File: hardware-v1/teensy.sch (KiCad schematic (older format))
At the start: 31 parts, among them J1 USB-MICRO-B-SHIELDED, P7 USB_POWER, P8 CORTEX_DEBUG, SW2 PROGRAM, U4 LP38691, U5 MK20DX256VLH7, U6 MKL02Z32VFG4, X1 CRYSTAL_SMD, Y1 32kHz

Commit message: Finalizing revB
 - Added part numbers on all parts (in kicad PartNumber field)
 - Some finicking in a bunch of corners
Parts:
- C10, C4, C5, C6: PartNumber (none) -> CC0603MRX5R5BB225
- C11, C12, C13, C14, C7, C8, C9: PartNumber (none) -> CC0603KPX7R7BB104
- D3: PartNumber (none) -> LTST-C190KFKT
- D4: PartNumber (none) -> LM4040QCEM3-3.0/NOPB
- J1: PartNumber (none) -> 10103592-0001LF
- L2, L3, L4: PartNumber (none) -> 742792651
- P7: PartNumber (none) -> PREC002SAAN-RC
- P8: PartNumber (none) -> 3220-10-0100-00
- R10: PartNumber (none) -> RC0603JR-072K4L
- R11: PartNumber (none) -> RC0603JR-07470RL
- R12: PartNumber (none) -> 311-0.0HRCT-ND
- R8, R9: PartNumber (none) -> RC0603JR-0733RL
- SW2: PartNumber (none) -> FSMSM
- U4: PartNumber (none) -> LP38691DTX-3.3/NOPB
- U5: PartNumber (none) -> MK20DX256VLH7
- X1: PartNumber (none) -> NX3225SA-16.000MHZ-STD-CSR-1
- Y1: PartNumber (none) -> CFV-20632000AZFB
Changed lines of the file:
@@
 F 2 "Housings_QFP:TQFP-64_10x10mm_Pitch0.5mm" H 8350 3550 60  0001 C CNN
 F 3 "" H 8350 3550 60  0000 C CNN
+F 4 "MK20DX256VLH7" H 7650 3300 60  0001 C CNN "PartNumber"
 	1    7650 3300
 	1    0    0    -1
@@
 F 2 "bb:SWITCH_SMD_3x6" H 3750 4900 60  0001 C CNN
 F 3 "" H 3750 4900 60  0000 C CNN
+F 4 "FSMSM" H 3750 4900 60  0001 C CNN "PartNumber"
 	1    3750 4900
 	1    0    0    -1
@@
 F 2 "bb:HEADER_2x5_0.05" H 2450 5000 60  0001 C CNN
 F 3 "" H 2450 5000 60  0000 C CNN
+F 4 "3220-10-0100-00" H 2450 6200 60  0001 C CNN "PartNumber"
 	1    2450 6200
 	1    0    0    -1
@@
 F 2 "Resistors_SMD:R_0603" V 1930 1350 30  0001 C CNN
 F 3 "" H 2000 1350 30  0000 C CNN
+F 4 "RC0603JR-0733RL" H 2000 1350 60  0001 C CNN "PartNumber"
 	1    2000 1350
 	0    -1   -1   0
@@
 F 2 "Resistors_SMD:R_0603" V 1930 1500 30  0001 C CNN
 F 3 "" H 2000 1500 30  0000 C CNN
+F 4 "RC0603JR-0733RL" H 2000 1500 60  0001 C CNN "PartNumber"
 	1    2000 1500
 	0    -1   -1   0
@@
 F 2 "Resistors_SMD:R_0603" H 1300 2050 60  0001 C CNN
 F 3 "" H 1300 2050 60  0000 C CNN
+F 4 "742792651" H 1300 2050 60  0001 C CNN "PartNumber"
 	1    1300 2050
 	0    1    1    0
@@
 F 2 "Capacitors_SMD:C_0603" H 6200 1600 60  0001 C CNN
 F 3 "" H 6200 1600 60  0000 C CNN
+F 4 "CC0603MRX5R5BB225" H 6200 1600 60  0001 C CNN "PartNumber"
 	1    6200 1600
 	1    0    0    -1
@@
 F 2 "Capacitors_SMD:C_0603" H 6000 1600 60  0001 C CNN
 F 3 "" H 6000 1600 60  0000 C CNN
+F 4 "CC0603KPX7R7BB104" H 6000 1600 60  0001 C CNN "PartNumber"
 	1    6000 1600
 	1    0    0    -1
@@
 F 2 "Capacitors_SMD:C_0603" H 5800 1600 60  0001 C CNN
 F 3 "" H 5800 1600 60  0000 C CNN
+F 4 "CC0603KPX7R7BB104" H 5800 1600 60  0001 C CNN "PartNumber"
 	1    5800 1600
 	1    0    0    -1
@@
 F 2 "Capacitors_SMD:C_0603" H 5600 1600 60  0001 C CNN
 F 3 "" H 5600 1600 60  0000 C CNN
+F 4 "CC0603KPX7R7BB104" H 5600 1600 60  0001 C CNN "PartNumber"
 	1    5600 1600
 	1    0    0    -1
@@
 F 2 "Resistors_SMD:R_0603" H 5200 1800 60  0001 C CNN
 F 3 "" H 5200 1800 60  0000 C CNN
+F 4 "742792651" H 5200 1800 60  0001 C CNN "PartNumber"
 	1    5200 1800
 	-1   0    0    1
@@
 F 2 "Resistors_SMD:R_0603" H 5300 3000 60  0001 C CNN
 F 3 "" H 5300 3000 60  0000 C CNN
+F 4 "742792651" H 5300 3000 60  0001 C CNN "PartNumber"
 	1    5300 3000
 	-1   0    0    1
@@
 F 2 "Resistors_SMD:R_0603" V 5630 2400 30  0001 C CNN
 F 3 "" H 5700 2400 30  0000 C CNN
+F 4 "RC0603JR-072K4L" H 5700 2400 60  0001 C CNN "PartNumber"
 	1    5700 2400
 	0    1    1    0
@@
 F 2 "Capacitors_SMD:C_0603" H 6450 2550 60  0001 C CNN
 F 3 "" H 6450 2550 60  0000 C CNN
+F 4 "CC0603KPX7R7BB104" H 6450 2550 60  0001 C CNN "PartNumber"
 	1    6450 2550
 	1    0    0    -1
@@
 F 2 "Capacitors_SMD:C_0603" H 5400 2550 60  0001 C CNN
 F 3 "" H 5400 2550 60  0000 C CNN
+F 4 "CC0603KPX7R7BB104" H 5400 2550 60  0001 C CNN "PartNumber"
 	1    5400 2550
 	1    0    0    -1
@@
 F 2 "bb:Crystal_Watch_6mm" H 6800 3400 60  0001 C CNN
 F 3 "" H 6800 3400 60  0000 C CNN
+F 4 "CFV-20632000AZFB" H 6800 3400 60  0001 C CNN "PartNumber"
 	1    6800 3400
 	0    1    1    0
@@
 F 2 "TO_SOT_Packages_SMD:TO-252-2Lead" H 3550 1400 60  0001 C CNN
 F 3 "" H 3550 1400 60  0000 C CNN
+F 4 "LP38691DTX-3.3/NOPB" H 3550 1400 60  0001 C CNN "PartNumber"
 	1    3550 1400
 	1    0    0    -1
@@
 F 2 "Capacitors_SMD:C_0603" H 4100 1550 60  0001 C CNN
 F 3 "" H 4100 1550 60  0000 C CNN
+F 4 "CC0603MRX5R5BB225" H 4100 1550 60  0001 C CNN "PartNumber"
 	1    4100 1550
 	1    0    0    -1
@@
 F 2 "Capacitors_SMD:C_0603" H 3000 1550 60  0001 C CNN
 F 3 "" H 3000 1550 60  0000 C CNN
+F 4 "CC0603MRX5R5BB225" H 3000 1550 60  0001 C CNN "PartNumber"
 	1    3000 1550
 	1    0    0    -1
@@
 F 2 "Capacitors_SMD:C_0603" H 1500 1050 60  0001 C CNN
 F 3 "" H 1500 1050 60  0000 C CNN
+F 4 "CC0603MRX5R5BB225" H 1500 1050 60  0001 C CNN "PartNumber"
 	1    1500 1050
 	1    0    0    -1
@@
 F 2 "LEDs:LED_0603" H 9450 2500 60  0001 C CNN
 F 3 "" H 9450 2500 60  0000 C CNN
+F 4 "LTST-C190KFKT" H 9450 2500 60  0001 C CNN "PartNumber"
 	1    9450 2500
 	-1   0    0    1
@@
 F 2 "Resistors_SMD:R_0603" V 9830 2500 30  0001 C CNN
 F 3 "" H 9900 2500 30  0000 C CNN
+F 4 "RC0603JR-07470RL" H 9900 2500 60  0001 C CNN "PartNumber"
 	1    9900 2500
 	0    -1   -1   0
@@
 F 2 "Pin_Headers:Pin_Header_Straight_1x02" H 1900 700 60  0001 C CNN
 F 3 "" H 1900 700 60  0000 C CNN
+F 4 "PREC002SAAN-RC" H 1900 700 60  0001 C CNN "PartNumber"
 	1    1900 700
 	0    -1   -1   0
@@
 F 2 "Capacitors_SMD:C_0603" H 5750 3500 60  0001 C CNN
 F 3 "" H 5750 3500 60  0000 C CNN
+F 4 "CC0603KPX7R7BB104" H 5750 3500 60  0001 C CNN "PartNumber"
 	1    5750 3500
 	1    0    0    -1
@@
 F 2 "gsg-modules:USB-MICROB-FCI-10103592-LONGPADS" H 1000 1450 60  0001 C CNN
 F 3 "" H 1000 1450 60  0000 C CNN
+F 4 "10103592-0001LF" H 1000 1450 60  0001 C CNN "PartNumber"
 	1    1000 1450
 	-1   0    0    -1
@@
 F 2 "bb:CRYSTAL-NX3225SA" H 6600 3100 60  0001 C CNN
 F 3 "" H 6600 3100 60  0000 C CNN
+F 4 "NX3225SA-16.000MHZ-STD-CSR-1" H 6600 3100 60  0001 C CNN "PartNumber"
 	1    6600 3100
 	1    0    0    -1
@@
 F 2 "Capacitors_SMD:C_0603" H 1350 3750 60  0001 C CNN
 F 3 "" H 1350 3750 60  0000 C CNN
+F 4 "CC0603KPX7R7BB104" H 1350 3750 60  0001 C CNN "PartNumber"
 	1    1350 3750
 	1    0    0    -1
@@
 F 2 "Resistors_SMD:R_0603" V 3180 3600 50  0001 C CNN
 F 3 "" H 3250 3600 50  0000 C CNN
+F 4 "311-0.0HRCT-ND " H 3250 3600 60  0001 C CNN "PartNumber"
 	1    3250 3600
 	0    1    1    0
@@
 F 2 "TO_SOT_Packages_SMD:SOT-23" H 6050 2550 50  0001 C CNN
 F 3 "" H 6050 2550 50  0000 C CNN
+F 4 "LM4040QCEM3-3.0/NOPB" H 6050 2550 60  0001 C CNN "PartNumber"
 	1    6050 2550
 	0    1    1    0

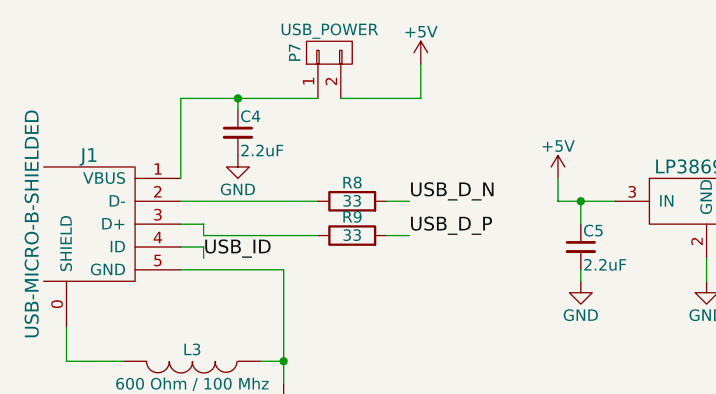
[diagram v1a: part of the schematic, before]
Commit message: adding oring diodes to schematic
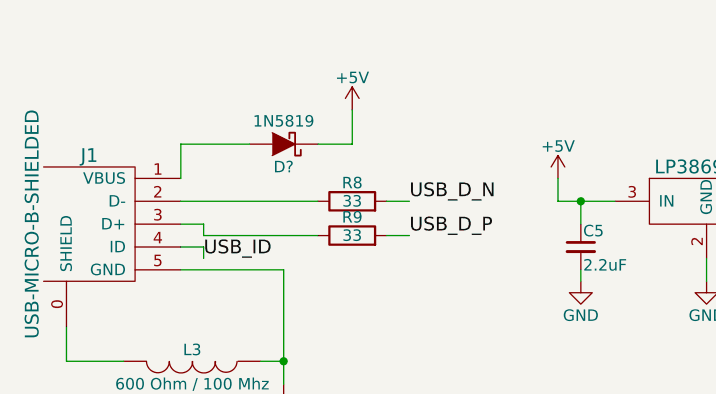
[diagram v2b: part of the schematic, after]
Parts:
- removed C4: 2.2uF, Capacitors_SMD:C_0603, symbol C_Small
- removed P7: USB_POWER, Pin_Headers:Pin_Header_Straight_1x02, symbol CONN_01X02
- added D?: 1N5819, Diodes_SMD:SOD-123, symbol D_Schottky
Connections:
- net +5V: now also D?.1 (K)
- net at J1.1 (VBUS): now also D?.2 (A)
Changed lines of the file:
@@
 L +5V #PWR042
 U 1 1 565AEF07
-P 2300 750
-F 0 "#PWR042" H 2300 600 50  0001 C CNN
-F 1 "+5V" H 2300 890 50  0000 C CNN
-F 2 "" H 2300 750 60  0000 C CNN
-F 3 "" H 2300 750 60  0000 C CNN
-	1    2300 750
-	1    0    0    -1
-$EndComp
-Wire Wire Line
-	1250 1250 1250 900
-Wire Wire Line
-	1250 900  1850 900
-$Comp
-L C_Small C4
-U 1 1 565B07F5
-P 1500 1050
-F 0 "C4" H 1510 1120 50  0000 L CNN
-F 1 "2.2uF" H 1510 970 50  0000 L CNN
-F 2 "Capacitors_SMD:C_0603" H 1500 1050 60  0001 C CNN
-F 3 "" H 1500 1050 60  0000 C CNN
-F 4 "CC0603MRX5R5BB225" H 1500 1050 60  0001 C CNN "PartNumber"
-	1    1500 1050
-	1    0    0    -1
-$EndComp
-$Comp
-L GND #PWR043
-U 1 1 565B08A1
-P 1500 1150
-F 0 "#PWR043" H 1500 900 50  0001 C CNN
-F 1 "GND" H 1500 1000 50  0000 C CNN
-F 2 "" H 1500 1150 60  0000 C CNN
-F 3 "" H 1500 1150 60  0000 C CNN
-	1    1500 1150
-	1    0    0    -1
-$EndComp
-Wire Wire Line
-	1500 900  1500 950
-Connection ~ 1500 900
+P 2000 950
+F 0 "#PWR042" H 2000 800 50  0001 C CNN
+F 1 "+5V" H 2000 1090 50  0000 C CNN
+F 2 "" H 2000 950 60  0000 C CNN
+F 3 "" H 2000 950 60  0000 C CNN
+	1    2000 950
+	1    0    0    -1
+$EndComp
 Text Label 6150 4100 2    60   ~ 0
 USB_ID
@@
 Wire Wire Line
 	8250 5300 8600 5300
-$Comp
-L CONN_01X02 P7
-U 1 1 565CA42D
-P 1900 700
-F 0 "P7" H 1900 850 50  0000 C CNN
-F 1 "USB_POWER" V 2000 700 50  0000 C CNN
-F 2 "Pin_Headers:Pin_Header_Straight_1x02" H 1900 700 60  0001 C CNN
-F 3 "" H 1900 700 60  0000 C CNN
-F 4 "PREC002SAAN-RC" H 1900 700 60  0001 C CNN "PartNumber"
-	1    1900 700
-	0    -1   -1   0
-$EndComp
-Wire Wire Line
-	1950 900  2300 900
-Wire Wire Line
-	2300 900  2300 750
+Wire Wire Line
+	2000 1100 2000 950
 Text HLabel 8600 1450 2    60   Input ~ 0
 23/A9
@@
 	1    0    0    -1
 $EndComp
+$Comp
+L D_Schottky D?
+U 1 1 56B7D3C5
+P 1700 1100
+F 0 "D?" H 1700 1200 50  0000 C CNN
+F 1 "1N5819" H 1700 1000 50  0000 C CNN
+F 2 "Diodes_SMD:SOD-123" H 1700 1100 60  0001 C CNN
+F 3 "" H 1700 1100 60  0000 C CNN
+F 4 "1N5819HW-7-F" H 1700 1100 60  0001 C CNN "PartNumber"
+	1    1700 1100
+	-1   0    0    1
+$EndComp
+Wire Wire Line
+	1250 1100 1550 1100
+Wire Wire Line
+	1850 1100 2000 1100
+Wire Wire Line
+	1250 1250 1250 1100
 $EndSCHEMATC

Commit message: Final touches + v1revb sent to oshpark
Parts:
- gave numbers to parts that had none: 1
- renumbered C11 to C10, C12 to C11, C13 to C12, C14 to C13, C5 to C4, C6 to C5, C7 to C6, C8 to C7, C9 to C8, C10 to C9, D3 to D5, D4 to D6, P8 to P6
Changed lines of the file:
@@
 DEBUG
 $Comp
-L CORTEX_DEBUG P8
+L CORTEX_DEBUG P6
 U 1 1 56590B49
 P 2450 6200
-F 0 "P8" H 2100 6500 50  0000 C CNN
+F 0 "P6" H 2100 6500 50  0000 C CNN
 F 1 "CORTEX_DEBUG" H 2600 6500 50  0000 C CNN
 F 2 "bb:HEADER_2x5_0.05" H 2450 5000 60  0001 C CNN
@@
 $EndComp
 $Comp
-L C_Small C10
+L C_Small C9
 U 1 1 56596486
 P 6200 1600
-F 0 "C10" H 6210 1670 50  0000 L CNN
+F 0 "C9" H 6210 1670 50  0000 L CNN
 F 1 "2.2uF" H 6210 1520 50  0000 L CNN
 F 2 "Capacitors_SMD:C_0603" H 6200 1600 60  0001 C CNN
@@
 $EndComp
 $Comp
-L C_Small C9
+L C_Small C8
 U 1 1 56596536
 P 6000 1600
-F 0 "C9" H 6010 1670 50  0000 L CNN
+F 0 "C8" H 6010 1670 50  0000 L CNN
 F 1 ".1uF" H 6010 1520 50  0000 L CNN
 F 2 "Capacitors_SMD:C_0603" H 6000 1600 60  0001 C CNN
@@
 $EndComp
 $Comp
-L C_Small C8
+L C_Small C7
 U 1 1 56596568
 P 5800 1600
-F 0 "C8" H 5810 1670 50  0000 L CNN
+F 0 "C7" H 5810 1670 50  0000 L CNN
 F 1 ".1uF" H 5810 1520 50  0000 L CNN
 F 2 "Capacitors_SMD:C_0603" H 5800 1600 60  0001 C CNN
@@
 $EndComp
 $Comp
-L C_Small C7
+L C_Small C6
 U 1 1 5659659D
 P 5600 1600
-F 0 "C7" H 5610 1670 50  0000 L CNN
+F 0 "C6" H 5610 1670 50  0000 L CNN
 F 1 ".1uF" H 5610 1520 50  0000 L CNN
 F 2 "Capacitors_SMD:C_0603" H 5600 1600 60  0001 C CNN
@@
 $EndComp
 $Comp
-L C_Small C12
+L C_Small C11
 U 1 1 56598B20
 P 6450 2550
-F 0 "C12" H 6460 2620 50  0000 L CNN
+F 0 "C11" H 6460 2620 50  0000 L CNN
 F 1 ".1uF" H 6460 2470 50  0000 L CNN
 F 2 "Capacitors_SMD:C_0603" H 6450 2550 60  0001 C CNN
@@
 USB_D_N
 $Comp
-L C_Small C11
+L C_Small C10
 U 1 1 56599D40
 P 5400 2550
-F 0 "C11" H 5410 2620 50  0000 L CNN
+F 0 "C10" H 5410 2620 50  0000 L CNN
 F 1 ".1uF" H 5410 2470 50  0000 L CNN
 F 2 "Capacitors_SMD:C_0603" H 5400 2550 60  0001 C CNN
@@
 	4250 1350 4250 1250
 $Comp
-L C_Small C6
+L C_Small C5
 U 1 1 565A6E2D
 P 4100 1550
-F 0 "C6" H 4110 1620 50  0000 L CNN
+F 0 "C5" H 4110 1620 50  0000 L CNN
 F 1 "2.2uF" H 4110 1470 50  0000 L CNN
 F 2 "Capacitors_SMD:C_0603" H 4100 1550 60  0001 C CNN
@@
 $EndComp
 $Comp
-L C_Small C5
+L C_Small C4
 U 1 1 565AC697
 P 3000 1550
-F 0 "C5" H 3010 1620 50  0000 L CNN
+F 0 "C4" H 3010 1620 50  0000 L CNN
 F 1 "2.2uF" H 3010 1470 50  0000 L CNN
 F 2 "Capacitors_SMD:C_0603" H 3000 1550 60  0001 C CNN
@@
 Connection ~ 6300 4000
 $Comp
-L LED D3
+L LED D5
 U 1 1 565BD891
 P 9450 2500
-F 0 "D3" H 9450 2600 50  0000 C CNN
+F 0 "D5" H 9450 2600 50  0000 C CNN
 F 1 "LED" H 9450 2400 50  0000 C CNN
 F 2 "LEDs:LED_0603" H 9450 2500 60  0001 C CNN
@@
 	8250 2450 8600 2450
 $Comp
-L GND #PWR044
+L GND #PWR043
 U 1 1 565BDF2E
 P 10200 2600
-F 0 "#PWR044" H 10200 2350 50  0001 C CNN
+F 0 "#PWR043" H 10200 2350 50  0001 C CNN
 F 1 "GND" H 10200 2450 50  0000 C CNN
 F 2 "" H 10200 2600 60  0000 C CNN
@@
 NoConn ~ 1800 4300
 $Comp
-L +3.3V #PWR045
+L +3.3V #PWR044
 U 1 1 567B1DAE
 P 5750 3300
-F 0 "#PWR045" H 5750 3150 50  0001 C CNN
+F 0 "#PWR044" H 5750 3150 50  0001 C CNN
 F 1 "+3.3V" H 5750 3440 50  0000 C CNN
 F 2 "" H 5750 3300 60  0000 C CNN
@@
 	6500 3550 7050 3550
 $Comp
-L C_Small C13
+L C_Small C12
 U 1 1 567B205D
 P 5750 3500
-F 0 "C13" H 5760 3570 50  0000 L CNN
+F 0 "C12" H 5760 3570 50  0000 L CNN
 F 1 ".1uF" H 5760 3420 50  0000 L CNN
 F 2 "Capacitors_SMD:C_0603" H 5750 3500 60  0001 C CNN
@@
 Connection ~ 5750 3350
 $Comp
-L GND #PWR046
+L GND #PWR045
 U 1 1 567B220D
 P 5750 3650
-F 0 "#PWR046" H 5750 3400 50  0001 C CNN
+F 0 "#PWR045" H 5750 3400 50  0001 C CNN
 F 1 "GND" H 5750 3500 50  0000 C CNN
 F 2 "" H 5750 3650 60  0000 C CNN
@@
 Connection ~ 5200 2250
 $Comp
-L PWR_FLAG #FLG047
+L PWR_FLAG #FLG046
 U 1 1 567B5BB9
 P 5550 2200
-F 0 "#FLG047" H 5550 2295 50  0001 C CNN
+F 0 "#FLG046" H 5550 2295 50  0001 C CNN
 F 1 "PWR_FLAG" H 5550 2380 50  0000 C CNN
 F 2 "" H 5550 2200 60  0000 C CNN
@@
 	6600 3200 6600 3300
 $Comp
-L GND #PWR048
+L GND #PWR047
 U 1 1 568579A5
 P 6600 3300
-F 0 "#PWR048" H 6600 3050 50  0001 C CNN
+F 0 "#PWR047" H 6600 3050 50  0001 C CNN
 F 1 "GND" H 6600 3150 50  0000 C CNN
 F 2 "" H 6600 3300 60  0000 C CNN
@@
 Connection ~ 1600 6150
 $Comp
-L GND #PWR049
+L GND #PWR048
 U 1 1 56858A76
 P 1100 6250
-F 0 "#PWR049" H 1100 6000 50  0001 C CNN
+F 0 "#PWR048" H 1100 6000 50  0001 C CNN
 F 1 "GND" H 1100 6100 50  0000 C CNN
 F 2 "" H 1100 6250 60  0000 C CNN
@@
 $EndComp
 $Comp
-L C_Small C14
+L C_Small C13
 U 1 1 565E3811
 P 1350 3750
-F 0 "C14" H 1360 3820 50  0000 L CNN
+F 0 "C13" H 1360 3820 50  0000 L CNN
 F 1 ".1uF" H 1360 3670 50  0000 L CNN
 F 2 "Capacitors_SMD:C_0603" H 1350 3750 60  0001 C CNN
@@
 DEBUG
 $Comp
-L ZENERsmall D4
+L ZENERsmall D6
 U 1 1 56ABEAB8
 P 6050 2550
-F 0 "D4" H 6050 2650 50  0000 C CNN
+F 0 "D6" H 6050 2650 50  0000 C CNN
 F 1 "LM4040QCEM3-3.0/NOPB" H 6050 2450 50  0000 C CNN
 F 2 "TO_SOT_Packages_SMD:SOT-23" H 6050 2550 50  0001 C CNN
@@
 $EndComp
 $Comp
-L D_Schottky D?
+L D_Schottky D4
 U 1 1 56B7D3C5
 P 1700 1100
-F 0 "D?" H 1700 1200 50  0000 C CNN
+F 0 "D4" H 1700 1200 50  0000 C CNN
 F 1 "1N5819" H 1700 1000 50  0000 C CNN
 F 2 "Diodes_SMD:SOD-123" H 1700 1100 60  0001 C CNN
